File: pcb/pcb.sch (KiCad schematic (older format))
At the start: 129 parts, among them J1 Conn_01x06, J2 SPI_Flash, SW1 Select, SW2 Done, U1 ATmega328P-AU, U2 DessinAfficheur, Y1 16Mhz

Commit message: add switch footprint
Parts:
- SW1, SW2: footprint (none) -> Button_Switch_SMD:SW_Push_1P1T_NO_6x6mm_H9.5mm
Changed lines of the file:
@@
 F 0 "SW1" H 10700 4585 50  0000 C CNN
 F 1 "Select" H 10700 4494 50  0000 C CNN
-F 2 "" H 10700 4500 50  0001 C CNN
+F 2 "Button_Switch_SMD:SW_Push_1P1T_NO_6x6mm_H9.5mm" H 10700 4500 50  0001 C CNN
 F 3 "~" H 10700 4500 50  0001 C CNN
 	1    10700 4300
@@
 F 0 "SW2" H 10700 5485 50  0000 C CNN
 F 1 "Done" H 10700 5394 50  0000 C CNN
-F 2 "" H 10700 5400 50  0001 C CNN
+F 2 "Button_Switch_SMD:SW_Push_1P1T_NO_6x6mm_H9.5mm" H 10700 5400 50  0001 C CNN
 F 3 "~" H 10700 5400 50  0001 C CNN
 	1    10700 5200

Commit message: add pcb leds
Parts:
- U2: footprint pasteur-lib:DessinAfficheurV3.1 -> pasteur-lib:DessinAfficheurV4.0
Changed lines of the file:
@@
 F 0 "U2" H 10800 6315 50  0000 C CNN
 F 1 "DessinAfficheur" H 10800 6224 50  0000 C CNN
-F 2 "pasteur-lib:DessinAfficheurV3.1" H 10800 6200 50  0001 C CNN
+F 2 "pasteur-lib:DessinAfficheurV4.0" H 10800 6200 50  0001 C CNN
 F 3 "" H 10800 6200 50  0001 C CNN
 	1    10800 6200

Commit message: fix i2c label
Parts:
- J1: value Conn_01x06 -> I2C_Data
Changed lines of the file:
@@
 P 10700 2850
 F 0 "J1" H 10780 2842 50  0000 L CNN
-F 1 "Conn_01x06" H 10780 2751 50  0000 L CNN
+F 1 "I2C_Data" H 10780 2751 50  0000 L CNN
 F 2 "Connector_PinSocket_2.54mm:PinSocket_1x06_P2.54mm_Vertical" H 10700 2850 50  0001 C CNN
 F 3 "~" H 10700 2850 50  0001 C CNN

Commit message: fix gnd of i2c
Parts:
- J1: footprint Connector_PinSocket_2.54mm:PinSocket_1x06_P2.54mm_Vertical -> Connector_PinSocket_2.54mm:PinSocket_1x05_P2.54mm_Vertical; symbol Connector_Generic:Conn_01x06 -> Connector_Generic:Conn_01x05
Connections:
- net GND: no longer J1.6 (Pin_6)
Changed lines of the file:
@@
 	10500 3050 10150 3050
 Connection ~ 10150 3050
-Wire Wire Line
-	10150 3050 10150 3150
 Text Notes 10500 3050 2    50   ~ 0
-GND
-Wire Wire Line
-	10500 3150 10150 3150
-Connection ~ 10150 3150
-Wire Wire Line
-	10150 3150 10150 4100
-Text Notes 10500 3150 2    50   ~ 0
 GND
 $Comp
@@
 NoConn ~ 8100 1600
 $Comp
-L Connector_Generic:Conn_01x06 J1
+L Connector_Generic:Conn_01x05 J1
 U 1 1 5EF857F3
 P 10700 2850
 F 0 "J1" H 10780 2842 50  0000 L CNN
 F 1 "I2C_Data" H 10780 2751 50  0000 L CNN
-F 2 "Connector_PinSocket_2.54mm:PinSocket_1x06_P2.54mm_Vertical" H 10700 2850 50  0001 C CNN
+F 2 "Connector_PinSocket_2.54mm:PinSocket_1x05_P2.54mm_Vertical" H 10700 2850 50  0001 C CNN
 F 3 "~" H 10700 2850 50  0001 C CNN
 	1    10700 2850
@@
 	1    0    0    -1
 $EndComp
+Wire Wire Line
+	10150 3050 10150 4100
 $EndSCHEMATC

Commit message: routing v1
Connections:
- net NL08: now reaches D43.2 (A), D44.1 (K), D45.2 (A), D46.1 (K), D47.2 (A), D48.1 (K), D49.2 (A), D50.1 (K), D51.2 (A), D52.1 (K), D53.2 (A), D54.1 (K), D55.2 (A), D56.1 (K), D57.1 (K), D58.2 (A), D75.1 (K), D76.2 (A), D95.1 (K), D96.2 (A), R8.2
- net NL01: now reaches D1.1 (K), D109.1 (K), D11.1 (K), D110.2 (A), D12.2 (A), D19.1 (K), D2.2 (A), D20.2 (A), D29.1 (K), D30.2 (A), D41.1 (K), D42.2 (A), D5.1 (K), D55.1 (K), D56.2 (A), D6.2 (A), D71.1 (K), D72.2 (A), D89.1 (K), D90.2 (A), R1.2
- net NL03: now reaches D105.1 (K), D106.2 (A), D15.1 (K), D16.2 (A), D25.1 (K), D26.2 (A), D3.2 (A), D37.1 (K), D38.2 (A), D4.1 (K), D5.2 (A), D51.1 (K), D52.2 (A), D6.1 (K), D67.1 (K), D68.2 (A), D7.1 (K), D8.2 (A), D85.1 (K), D86.2 (A), R3.2
- net NL04: now reaches D10.1 (K), D103.1 (K), D104.2 (A), D11.2 (A), D12.1 (K), D13.1 (K), D14.2 (A), D23.1 (K), D24.2 (A), D35.1 (K), D36.2 (A), D49.1 (K), D50.2 (A), D65.1 (K), D66.2 (A), D7.2 (A), D8.1 (K), D83.1 (K), D84.2 (A), D9.2 (A), R4.2
- net NL05: now reaches D101.1 (K), D102.2 (A), D13.2 (A), D14.1 (K), D15.2 (A), D16.1 (K), D17.2 (A), D18.1 (K), D19.2 (A), D20.1 (K), D21.1 (K), D22.2 (A), D33.1 (K), D34.2 (A), D47.1 (K), D48.2 (A), D63.1 (K), D64.2 (A), D81.1 (K), D82.2 (A), R5.2
- net NL06: now reaches D100.2 (A), D21.2 (A), D22.1 (K), D23.2 (A), D24.1 (K), D25.2 (A), D26.1 (K), D27.2 (A), D28.1 (K), D29.2 (A), D30.1 (K), D31.1 (K), D32.2 (A), D45.1 (K), D46.2 (A), D61.1 (K), D62.2 (A), D79.1 (K), D80.2 (A), D99.1 (K), R6.2
- net NL07: now reaches D31.2 (A), D32.1 (K), D33.2 (A), D34.1 (K), D35.2 (A), D36.1 (K), D37.2 (A), D38.1 (K), D39.2 (A), D40.1 (K), D41.2 (A), D42.1 (K), D43.1 (K), D44.2 (A), D59.1 (K), D60.2 (A), D77.1 (K), D78.2 (A), D97.1 (K), D98.2 (A), R7.2
- net NL09: now reaches D57.2 (A), D58.1 (K), D59.2 (A), D60.1 (K), D61.2 (A), D62.1 (K), D63.2 (A), D64.1 (K), D65.2 (A), D66.1 (K), D67.2 (A), D68.1 (K), D69.2 (A), D70.1 (K), D71.2 (A), D72.1 (K), D73.1 (K), D74.2 (A), D93.1 (K), D94.2 (A), R9.2
- net NL10: now reaches D73.2 (A), D74.1 (K), D75.2 (A), D76.1 (K), D77.2 (A), D78.1 (K), D79.2 (A), D80.1 (K), D81.2 (A), D82.1 (K), D83.2 (A), D84.1 (K), D85.2 (A), D86.1 (K), D87.2 (A), D88.1 (K), D89.2 (A), D90.1 (K), D92.2 (A), R10.2
- net NL11: now reaches D100.1 (K), D101.2 (A), D102.1 (K), D103.2 (A), D104.1 (K), D105.2 (A), D106.1 (K), D107.2 (A), D108.1 (K), D109.2 (A), D110.1 (K), D92.1 (K), D93.2 (A), D94.1 (K), D95.2 (A), D96.1 (K), D97.2 (A), D98.1 (K), D99.2 (A), R11.2
- net NL02: now reaches D1.2 (A), D10.2 (A), D107.1 (K), D108.2 (A), D17.1 (K), D18.2 (A), D2.1 (K), D27.1 (K), D28.2 (A), D3.1 (K), D39.1 (K), D4.2 (A), D40.2 (A), D53.1 (K), D54.2 (A), D69.1 (K), D70.2 (A), D87.1 (K), D88.2 (A), D9.1 (K), R2.2
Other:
- note removed: "NL01"
- note removed: "NL02"
- note removed: "NL03"
- note removed: "NL04"
- note removed: "NL05"
- note removed: "NL06"
- note removed: "NL07"
- note removed: "NL08"
- note removed: "NL09"
- note removed: "NL10"
- note removed: "NL11"
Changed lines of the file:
@@
 	7250 1550 7150 1550
 Connection ~ 7250 1550
-Wire Wire Line
-	7250 1550 7250 750
 Connection ~ 7150 1550
 Wire Wire Line
@@
 	7050 1250 7150 1250
 Connection ~ 7150 1250
-Wire Wire Line
-	7150 1250 7450 1250
 Wire Wire Line
 	6450 5600 6550 5600
@@
 	7150 5800 7450 5800
 Connection ~ 7150 5800
-Text Notes 7450 750  2    50   ~ 0
-NL01
-Text Notes 7450 1250 2    50   ~ 0
-NL02
-Text Notes 7450 1800 2    50   ~ 0
-NL03
-Text Notes 7450 2300 2    50   ~ 0
-NL04
-Text Notes 7450 2800 2    50   ~ 0
-NL05
-Text Notes 7450 3300 2    50   ~ 0
-NL06
-Text Notes 7450 3800 2    50   ~ 0
-NL07
-Text Notes 7450 4300 2    50   ~ 0
-NL08
-Text Notes 7450 4800 2    50   ~ 0
-NL09
-Text Notes 7450 5300 2    50   ~ 0
-NL10
-Text Notes 7450 5800 2    50   ~ 0
-NL11
 $Comp
 L Device:R_US R1
@@
 Wire Wire Line
 	10150 3050 10150 4100
+Text Label 7300 750  0    50   ~ 0
+NL01
+Wire Wire Line
+	7150 1250 7450 1250
+Wire Wire Line
+	7250 1550 7250 750
+Text Label 7300 1250 0    50   ~ 0
+NL02
+Text Label 7300 1800 0    50   ~ 0
+NL03
+Text Label 7300 2300 0    50   ~ 0
+NL04
+Text Label 7300 2800 0    50   ~ 0
+NL05
+Text Label 7300 3300 0    50   ~ 0
+NL06
+Text Label 7300 3800 0    50   ~ 0
+NL07
+Text Label 7300 4300 0    50   ~ 0
+NL08
+Text Label 7300 4800 0    50   ~ 0
+NL09
+Text Label 7300 5300 0    50   ~ 0
+NL10
+Text Label 7300 5800 0    50   ~ 0
+NL11
 $EndSCHEMATC

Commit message: clean footprints and update bom
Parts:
- D1, D10, D100, D101, D102, D103, D104, D105, D106, D107, D108, D109, D11, D110, D12, D13, D14, D15, D16, D17, D18, D19, D2, D20, D21, D22, D23, D24, D25, D26, D27, D28, D29, D3, D30, D31, D32, D33, D34, D35, D36, D37, D38, D39, D4, D40, D41, D42, D43, D44, D45, D46, D47, D48, D49, D5, D50, D51, D52, D53, D54, D55, D56, D57, D58, D59, D6, D60, D61, D62, D63, D64, D65, D66, D67, D68, D69, D7, D70, D71, D72, D73, D74, D75, D76, D77, D78, D79, D8, D80, D81, D82, D83, D84, D85, D86, D87, D88, D89, D9, D90, D92, D93, D94, D95, D96, D97, D98, D99: footprint LED_SMD:LED_0603_1608Metric -> pasteur-lib:LED_0603_1608Metric_smallfont
- J1: footprint Connector_PinSocket_2.54mm:PinSocket_1x05_P2.54mm_Vertical -> pasteur-lib:PinSocket_1x05_P2.54mm_Vertical_smallfont
- J2: footprint Connector_PinSocket_2.54mm:PinSocket_1x07_P2.54mm_Vertical -> pasteur-lib:PinSocket_1x07_P2.00mm_Horizontal_smallfont
- R1, R10, R11, R12, R13, R2, R3, R4, R5, R6, R7, R8, R9: footprint Resistor_SMD:R_0603_1608Metric -> pasteur-lib:R_0603_1608Metric_smallfont
- SW1, SW2: footprint Button_Switch_SMD:SW_Push_1P1T_NO_6x6mm_H9.5mm -> pasteur-lib:SW_Push_1P1T_NO_6x6mm_H9.5mm_smallfont
- Y1: footprint Crystal:Crystal_SMD_0603-2Pin_6.0x3.5mm -> pasteur-lib:Crystal_SMD_0603-2Pin_6.0x3.5mm_smallfont

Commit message: Update Library
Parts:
- U2: value DessinAfficheur -> HotelPasteur-V4.0
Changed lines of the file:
@@
 P 10800 6200
 F 0 "U2" H 10800 6315 50  0000 C CNN
-F 1 "DessinAfficheur" H 10800 6224 50  0000 C CNN
+F 1 "HotelPasteur-V4.0" H 10800 6224 50  0000 C CNN
 F 2 "pasteur-lib:DessinAfficheurV4.0" H 10800 6200 50  0001 C CNN
 F 3 "" H 10800 6200 50  0001 C CNN

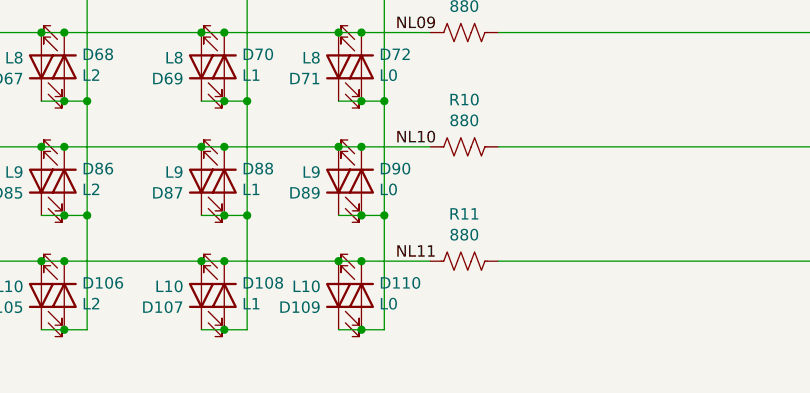
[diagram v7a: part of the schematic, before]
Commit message: Fix LED naming and parsing script for SMD components
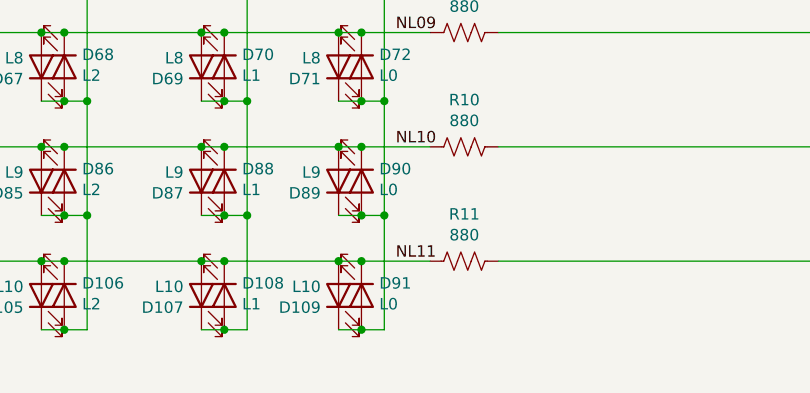
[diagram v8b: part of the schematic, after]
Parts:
- renumbered D110 to D91
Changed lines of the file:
@@
 $EndComp
 $Comp
-L Device:LED D110
+L Device:LED D91
 U 1 1 5DEA5D83
 P 7150 5950
-F 0 "D110" V 7097 6028 50  0000 L CNN
+F 0 "D91" V 7097 6028 50  0000 L CNN
 F 1 "L0" V 7188 6028 50  0000 L CNN
 F 2 "pasteur-lib:LED_0603_1608Metric_smallfont" H 7150 5950 50  0001 C CNN
